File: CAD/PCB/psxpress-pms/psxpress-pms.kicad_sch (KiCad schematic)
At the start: 42 parts, among them IC1 BQ25606RGER, IC2 MAX16054AZT+T, IC3 TPS61023DRLT, IC4 TPS564255DRLR, Q1 AONR21117, SW1 SW_SPST

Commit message: pms - optimize regulator layout & add 3D models for inductors
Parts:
- Q1: footprint (none) -> TRANS_AONR21321:TRANS_AONR21321
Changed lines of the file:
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@@
       (effects (font (size 1.27 1.27)))
     )
-    (property "Footprint" "" (at 172.72 100.33 0)
+    (property "Footprint" "TRANS_AONR21321:TRANS_AONR21321" (at 172.72 100.33 0)
       (effects (font (size 1.27 1.27)) hide)
     )

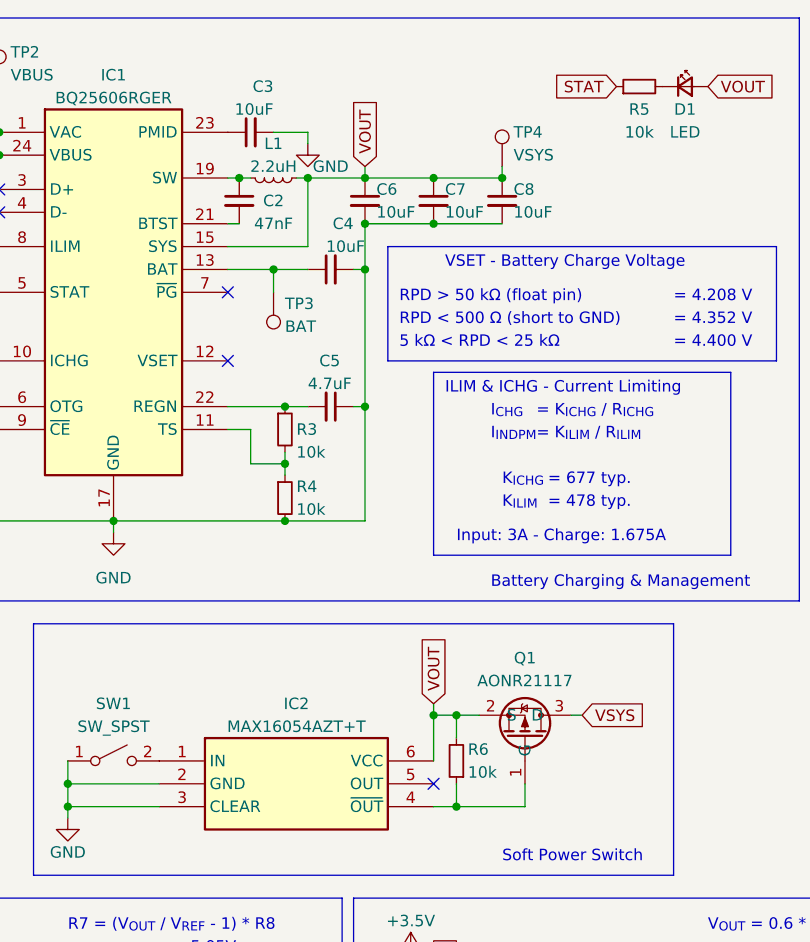
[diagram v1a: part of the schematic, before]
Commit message: pms - route BQ chip, finalize board footprint, & start optimizing
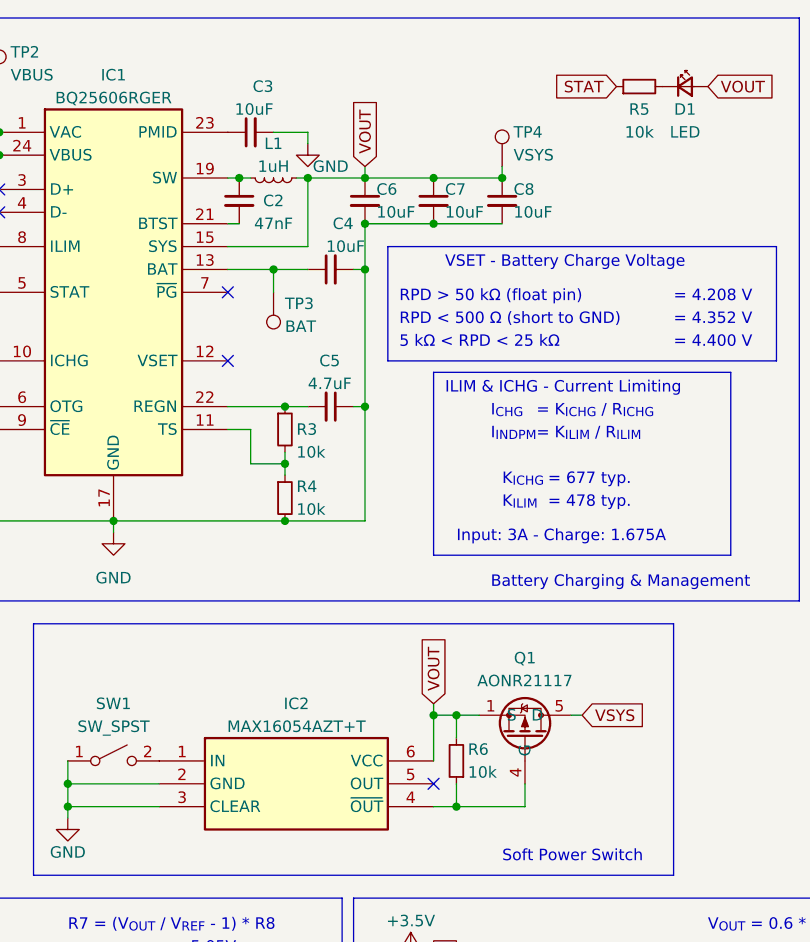
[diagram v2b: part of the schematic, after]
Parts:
- L1: value 2.2uH -> 1uH; footprint (none) -> Inductor_SMD:L_Taiyo-Yuden_MD-4040
- SW1: footprint (none) -> solderpads:pwr_switch_1.25mm_2
- TP1, TP3, TP5, TP6, TP7, TP8: footprint solderpads:power_pad_2.5x1.5mm -> solderpads:hipower_2.5x1.5mm
- TP2: footprint (none) -> solderpads:hipower_2.5x1.5mm
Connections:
- net VOUT: now also Q1.1 (S), Q1.3 (S)
- net VSYS: now also Q1.5 (D), Q1.6 (D), Q1.7 (D), Q1.8 (D), Q1.9 (D), Q1.9_1 (D), Q1.9_2 (D); no longer Q1.3 (D)
- net at IC2.4 (~{OUT}), R6.1: now also Q1.4 (G); no longer Q1.1 (G)
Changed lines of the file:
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@@
       (effects (font (size 1.27 1.27)) hide)
     )
+    (pin "4")
+    (pin "5")
+    (pin "6")
+    (pin "7")
+    (pin "8")
+    (pin "9")
+    (pin "9_1")
+    (pin "9_2")
     (pin "1")
     (pin "2")
@@
       (effects (font (size 1.27 1.27)) (justify left))
     )
-    (property "Footprint" "solderpads:power_pad_2.5x1.5mm" (at 78.74 128.27 0)
+    (property "Footprint" "solderpads:hipower_2.5x1.5mm" (at 78.74 128.27 0)
       (effects (font (size 1.27 1.27)) hide)
     )
@@
       (effects (font (size 1.27 1.27)) (justify right))
     )
-    (property "Footprint" "solderpads:power_pad_2.5x1.5mm" (at 87.63 135.89 0)
+    (property "Footprint" "solderpads:hipower_2.5x1.5mm" (at 87.63 135.89 0)
       (effects (font (size 1.27 1.27)) hide)
     )
@@
       (effects (font (size 1.27 1.27)) (justify right))
     )
-    (property "Footprint" "solderpads:power_pad_2.5x1.5mm" (at 134.62 53.34 0)
+    (property "Footprint" "solderpads:hipower_2.5x1.5mm" (at 134.62 53.34 0)
       (effects (font (size 1.27 1.27)) hide)
     )
@@
       (effects (font (size 1.27 1.27)) (justify right))
     )
-    (property "Footprint" "solderpads:power_pad_2.5x1.5mm" (at 97.79 80.01 0)
+    (property "Footprint" "solderpads:hipower_2.5x1.5mm" (at 97.79 80.01 0)
       (effects (font (size 1.27 1.27)) hide)
     )
@@
       (effects (font (size 1.27 1.27)) (justify right))
     )
-    (property "Footprint" "solderpads:power_pad_2.5x1.5mm" (at 157.48 135.89 0)
+    (property "Footprint" "solderpads:hipower_2.5x1.5mm" (at 157.48 135.89 0)
       (effects (font (size 1.27 1.27)) hide)
     )
@@
       (effects (font (size 1.27 1.27)) (justify left))
     )
-    (property "Footprint" "" (at 114.3 30.48 0)
+    (property "Footprint" "solderpads:hipower_2.5x1.5mm" (at 114.3 30.48 0)
       (effects (font (size 1.27 1.27)) hide)
     )
@@
       (effects (font (size 1.27 1.27)))
     )
-    (property "Footprint" "" (at 121.92 105.41 0)
+    (property "Footprint" "solderpads:pwr_switch_1.25mm_2" (at 121.92 105.41 0)
       (effects (font (size 1.27 1.27)) hide)
     )
@@
       (effects (font (size 1.27 1.27)) (justify left))
     )
-    (property "Footprint" "solderpads:power_pad_2.5x1.5mm" (at 149.86 128.27 0)
+    (property "Footprint" "solderpads:hipower_2.5x1.5mm" (at 149.86 128.27 0)
       (effects (font (size 1.27 1.27)) hide)
     )
@@
   )
   (symbol (lib_id "Device:L_Small") (at 139.7 40.64 270) (unit 1)
-    (in_bom yes) (on_board yes) (dnp no) (fields_autoplaced)
+    (in_bom yes) (on_board yes) (dnp no)
     (property "Reference" "L1" (at 139.7 36.83 90)
       (effects (font (size 1.27 1.27)))
     )
-    (property "Value" "2.2uH" (at 139.7 39.37 90)
-      (effects (font (size 1.27 1.27)))
-    )
-    (property "Footprint" "" (at 139.7 40.64 0)
-      (effects (font (size 1.27 1.27)) hide)
-    )
+    (property "Value" "1uH" (at 139.7 39.37 90)
+      (effects (font (size 1.27 1.27)))
+    )
+    (property "Footprint" "Inductor_SMD:L_Taiyo-Yuden_MD-4040" (at 139.7 40.64 0)
+      (effects (font (size 1.27 1.27)) hide)
+    )

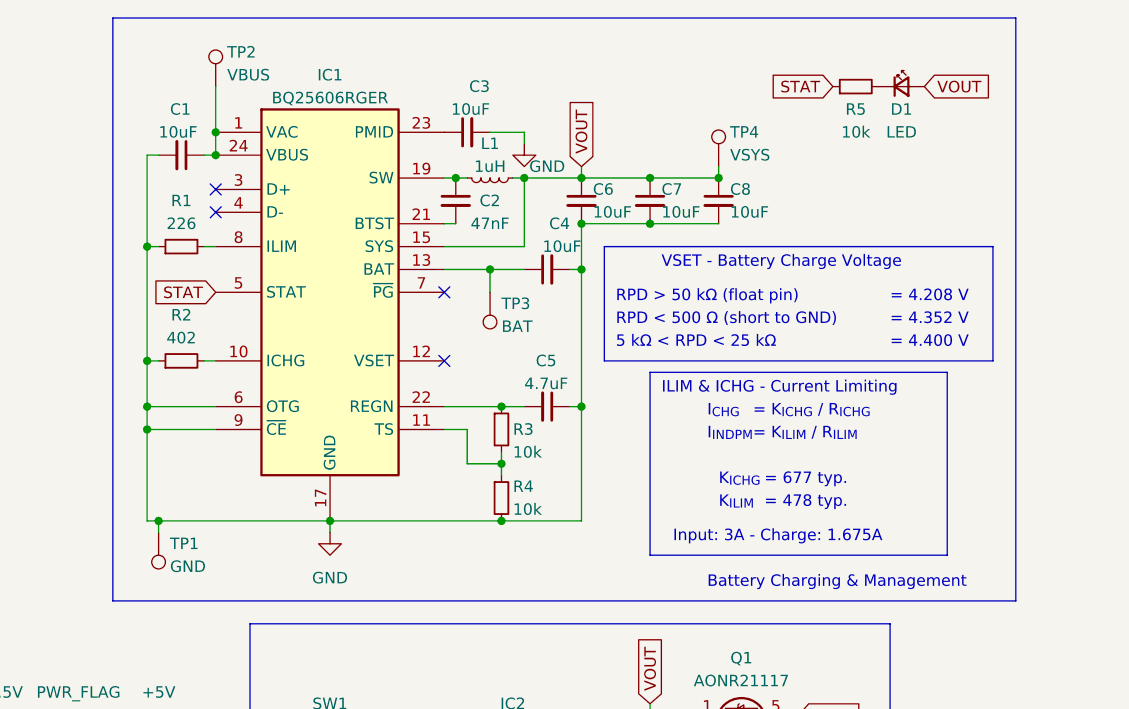
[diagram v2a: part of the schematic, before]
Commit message: pms - finish optimizing  - board complete
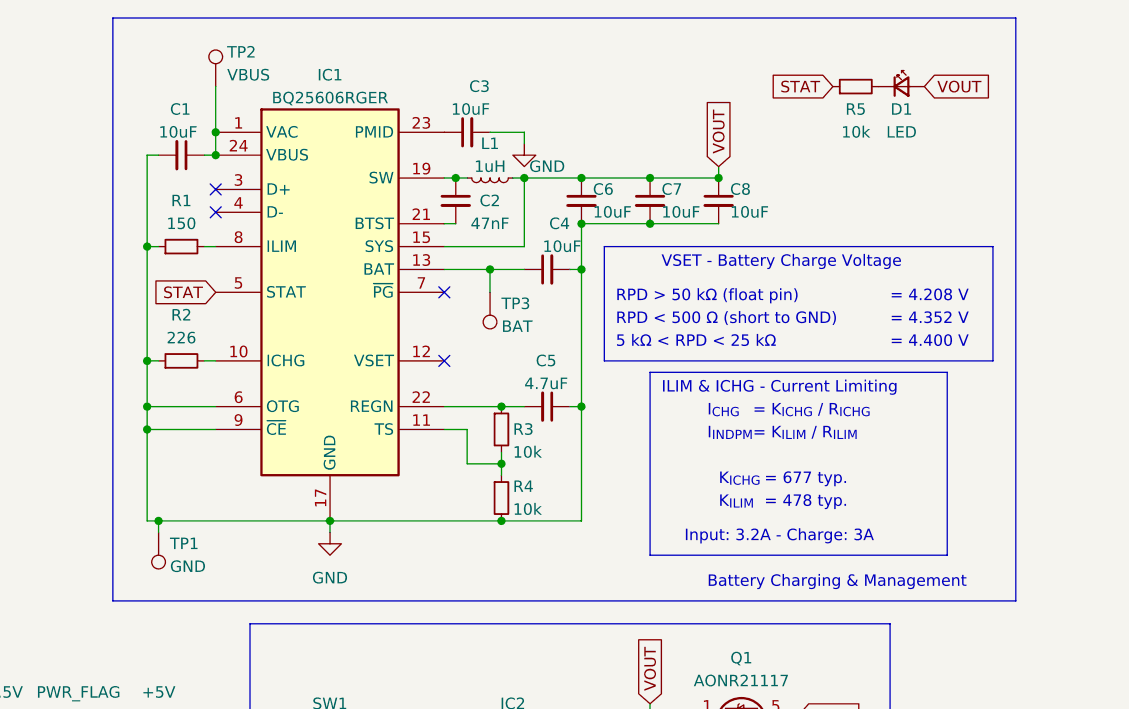
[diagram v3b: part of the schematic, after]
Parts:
- removed TP4: VSYS, symbol Connector:TestPoint
- D1: footprint (none) -> solderpads:led_1.25mm_2
- R1: value 226 -> 150
- R2: value 402 -> 226
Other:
- note added: "Input: 3.2A - Charge: 3A"
- note removed: "Input: 3A - Charge: 1.675A"
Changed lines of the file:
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@@
   (junction (at 140.97 72.39) (diameter 0) (color 0 0 0 0)
   )
+  (junction (at 140.97 66.04) (diameter 0) (color 0 0 0 0)
+  )
+  (junction (at 138.43 135.89) (diameter 0) (color 0 0 0 0)
+  )
+  (junction (at 121.92 78.74) (diameter 0) (color 0 0 0 0)
+  )
+  (junction (at 149.86 40.64) (diameter 0) (color 0 0 0 0)
+  )
+  (junction (at 160.02 100.33) (diameter 0) (color 0 0 0 0)
+  )
   (junction (at 165.1 40.64) (diameter 0) (color 0 0 0 0)
-  )
-  (junction (at 140.97 66.04) (diameter 0) (color 0 0 0 0)
-  )
-  (junction (at 138.43 135.89) (diameter 0) (color 0 0 0 0)
-  )
-  (junction (at 121.92 78.74) (diameter 0) (color 0 0 0 0)
-  )
-  (junction (at 149.86 40.64) (diameter 0) (color 0 0 0 0)
-  )
-  (junction (at 160.02 100.33) (diameter 0) (color 0 0 0 0)
   )
   (junction (at 149.86 45.72) (diameter 0) (color 0 0 0 0)
@@
   (no_connect (at 189.23 137.16))
   (no_connect (at 109.22 44.45))
-  (wire (pts (xy 149.86 39.37) (xy 149.86 40.64))
-    (stroke (width 0) (type default))
-  )
   (wire (pts (xy 116.84 105.41) (xy 116.84 107.95))
     (stroke (width 0) (type default))
@@
     (stroke (width 0) (type default))
   )
+  (wire (pts (xy 165.1 39.37) (xy 165.1 40.64))
+    (stroke (width 0) (type default))
+  )
   (wire (pts (xy 101.6 60.96) (xy 101.6 66.04))
     (stroke (width 0) (type default))
@@
   )
   (wire (pts (xy 139.7 50.8) (xy 143.51 50.8))
-    (stroke (width 0) (type default))
-  )
-  (wire (pts (xy 165.1 39.37) (xy 165.1 40.64))
     (stroke (width 0) (type default))
   )
@@
     (effects (font (size 1.27 1.27)) (justify left bottom))
   )
-  (text "Input: 3A - Charge: 1.675A" (at 160.02 81.28 0)
+  (text "Input: 3.2A - Charge: 3A" (at 161.29 81.28 0)
     (effects (font (size 1.27 1.27)) (justify left bottom))
   )
@@
     (effects (font (size 1.27 1.27)) (justify left bottom))
   )
-  (global_label "VOUT" (shape input) (at 149.86 39.37 90) (fields_autoplaced)
+  (global_label "VOUT" (shape input) (at 165.1 39.37 90) (fields_autoplaced)
     (effects (font (size 1.27 1.27)) (justify left))
-    (property "Intersheetrefs" "${INTERSHEET_REFS}" (at 149.86 31.747 90)
+    (property "Intersheetrefs" "${INTERSHEET_REFS}" (at 165.1 31.747 90)
       (effects (font (size 1.27 1.27)) (justify left) hide)
     )
@@
       (effects (font (size 1.27 1.27)))
     )
-    (property "Value" "402" (at 105.41 58.42 90)
+    (property "Value" "226" (at 105.41 58.42 90)
       (effects (font (size 1.27 1.27)))
     )
@@
       (effects (font (size 1.27 1.27)))
     )
-    (property "Value" "226" (at 105.41 45.72 90)
+    (property "Value" "150" (at 105.41 45.72 90)
       (effects (font (size 1.27 1.27)))
     )
@@
     )
   )
-  (symbol (lib_id "Connector:TestPoint") (at 165.1 39.37 0) (unit 1)
-    (in_bom yes) (on_board yes) (dnp no)
-    (property "Reference" "TP4" (at 166.37 35.56 0)
-      (effects (font (size 1.27 1.27)) (justify left))
-    )
-    (property "Value" "VSYS" (at 166.37 38.1 0)
-      (effects (font (size 1.27 1.27)) (justify left))
-    )
-    (property "Footprint" "" (at 170.18 39.37 0)
-      (effects (font (size 1.27 1.27)) hide)
-    )
-    (property "Datasheet" "~" (at 170.18 39.37 0)
-      (effects (font (size 1.27 1.27)) hide)
-    )
-    (pin "1")
-    (instances
-      (project "psxpress-pms"
-        (path "/b46ebcbe-5ef3-41ff-bf92-95c75415e5a2"
-          (reference "TP4") (unit 1)
-        )
-      )
-    )
-  )
   (symbol (lib_id "power:GND") (at 195.58 148.59 0) (unit 1)
     (in_bom yes) (on_board yes) (dnp no) (fields_autoplaced)
@@
       (effects (font (size 1.27 1.27)))
     )
-    (property "Footprint" "" (at 185.42 30.48 90)
-      (effects (font (size 1.27 1.27)) hide)
-    )
+    (property "Footprint" "solderpads:led_1.25mm_2" (at 185.42 30.48 90)
+      (effects (font (size 1.27 1.27)) hide)
+    )

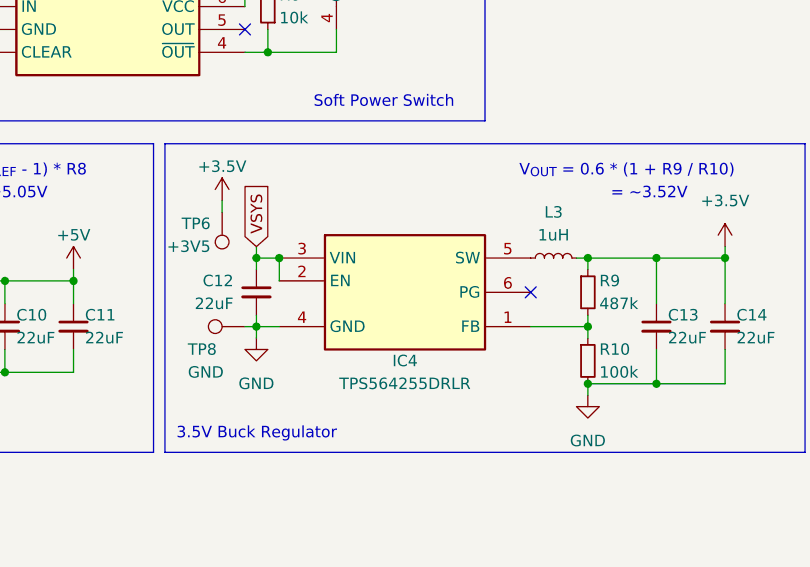
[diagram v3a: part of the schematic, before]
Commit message: pms - update schematic with fixed TPS564255 symbol
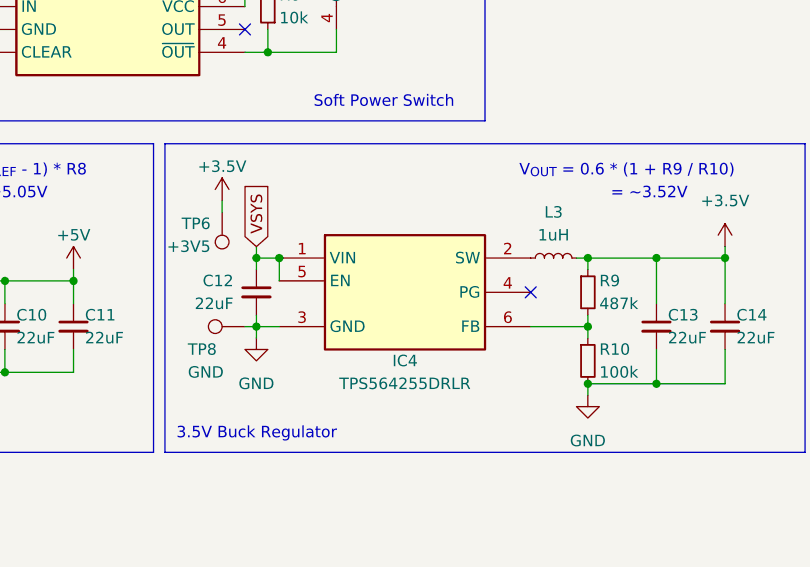
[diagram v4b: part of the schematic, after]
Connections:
- net GND: now also IC4.3 (GND); no longer IC4.4 (GND)
- net VSYS: now also IC4.1 (VIN), IC4.5 (EN); no longer IC4.2 (EN), IC4.3 (VIN)
- net at R10.1, R9.2: now also IC4.6 (FB); no longer IC4.1 (FB)
- net at L3.1: now also IC4.2 (SW); no longer IC4.5 (SW)
